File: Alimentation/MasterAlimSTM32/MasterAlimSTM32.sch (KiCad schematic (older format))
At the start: 74 parts, among them J1 Ext-Con, J10 Interf-Reg1, J11 AU Logic, J12 Interf-Reg2, J13 Interf-Reg3, J14 Interf-Reg4, J2 5V, J3 Bat. IN, J4 SWD, J5 Direct Out, J6 Reg 1, J7 Reg 2, J8 Reg 3, J9 Reg 4, SW1 SW_SPDT, U1 PTN78060W_EUW-7, U2 STM32F405RGTx, U3 ACS712xLCTR-20A, Y1 16Mhz

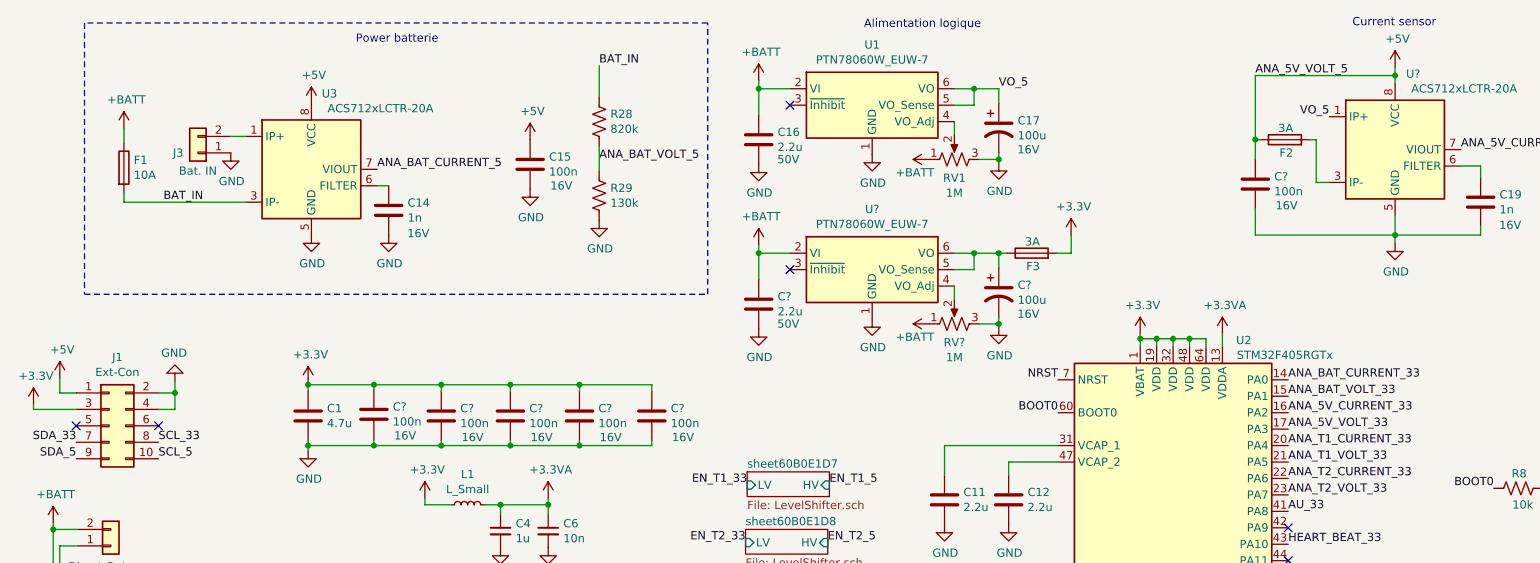
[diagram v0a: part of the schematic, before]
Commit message: Module alim ISO, clean master alim
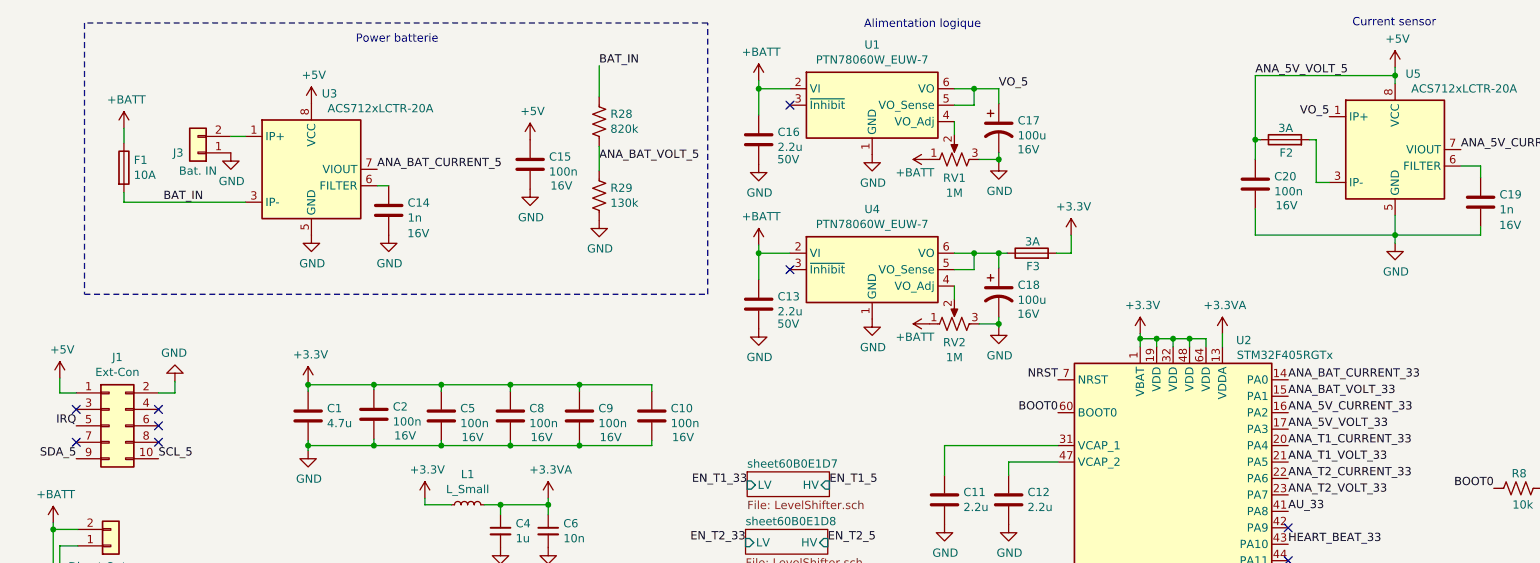
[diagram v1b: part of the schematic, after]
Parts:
- C14: LCSC C163169 -> (none)
- U1: footprint Module:Texas_EUW_R-PDSS-T7_THT -> ARIG:Texas_EUW_R-PDSS-T7_THT
- U4: renamed from U?; footprint Module:Texas_EUW_R-PDSS-T7_THT -> ARIG:Texas_EUW_R-PDSS-T7_THT
- gave numbers to parts that had none: 10
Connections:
- net +3V3: no longer J1.3 (Pin_3)
- net GND: no longer J1.4 (Pin_4)
- net SCL_33: no longer J1.8 (Pin_8)
- net SDA_33: no longer J1.7 (Pin_7)
- net IRQ: now reaches J1.5 (Pin_5)
- no-connect marks 32 -> 35
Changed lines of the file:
@@
 F 3 "~" H 2740 1700 50  0001 C CNN
 F 4 "16V" H 2920 1560 50  0000 C CNN "Tension"
-F 5 "C163169" H 2740 1700 50  0001 C CNN "LCSC"
-F 6 "C163169" H 2740 1700 50  0001 C CNN "LCSC Part"
+F 5 "C163169" H 2740 1700 50  0001 C CNN "LCSC Part"
 	1    2740 1700
 	1    0    0    -1
@@
 	1    0    0    -1
 $EndComp
-NoConn ~ 840  3010
 $Comp
 L MCU_ST_STM32F4:STM32F405RGTx U2
@@
 F 0 "U1" H 5680 1427 50  0000 C CNN
 F 1 "PTN78060W_EUW-7" H 5680 1336 50  0000 C CNN
-F 2 "Module:Texas_EUW_R-PDSS-T7_THT" H 5580 660 50  0001 C CNN
+F 2 "ARIG:Texas_EUW_R-PDSS-T7_THT" H 5580 660 50  0001 C CNN
 F 3 "https://www.ti.com/lit/ds/symlink/ptn78060w.pdf" H 5655 1110 50  0001 C CNN
 F 4 "" H 5680 1060 50  0001 C CNN "LCSC Bom"
@@
 Wire Wire Line
 	9500 4690 9580 4690
-Text Label 1340 3110 0    50   ~ 0
-SCL_33
-Text Label 840  3110 2    50   ~ 0
-SDA_33
-$Comp
-L power:+3.3V #PWR0148
-U 1 1 609CF06D
-P 580 2880
-F 0 "#PWR0148" H 580 2730 50  0001 C CNN
-F 1 "+3.3V" H 595 3053 50  0000 C CNN
-F 2 "" H 580 2880 50  0001 C CNN
-F 3 "" H 580 2880 50  0001 C CNN
-	1    580  2880
-	1    0    0    -1
-$EndComp
-Wire Wire Line
-	580  2880 580  2910
-Wire Wire Line
-	580  2910 840  2910
-Wire Wire Line
-	1440 2810 1440 2910
-Wire Wire Line
-	1440 2910 1340 2910
-Connection ~ 1440 2810
 $Comp
 L Device:R_US R4
@@
 	6510 3230 6510 3310
 $Comp
-L Device:C C?
+L Device:C C20
 U 1 1 5FC94B59
 P 8010 1540
-F 0 "C?" H 7895 1494 50  0000 R CNN
+F 0 "C20" H 7895 1494 50  0000 R CNN
 F 1 "100n" H 7895 1585 50  0000 R CNN
 F 2 "Capacitor_SMD:C_0603_1608Metric_Pad1.08x0.95mm_HandSolder" H 8048 1390 50  0001 C CNN
@@
 $EndComp
 $Comp
-L Device:C C?
+L Device:C C2
 U 1 1 5FC9E5DA
 P 2650 2940
-F 0 "C?" H 2535 2894 50  0000 R CNN
+F 0 "C2" H 2535 2894 50  0000 R CNN
 F 1 "100n" H 2535 2985 50  0000 R CNN
 F 2 "Capacitor_SMD:C_0603_1608Metric_Pad1.08x0.95mm_HandSolder" H 2688 2790 50  0001 C CNN
@@
 $EndComp
 $Comp
-L Device:C C?
+L Device:C C5
 U 1 1 5FC9F7C9
 P 3060 2950
-F 0 "C?" H 2945 2904 50  0000 R CNN
+F 0 "C5" H 2945 2904 50  0000 R CNN
 F 1 "100n" H 2945 2995 50  0000 R CNN
 F 2 "Capacitor_SMD:C_0603_1608Metric_Pad1.08x0.95mm_HandSolder" H 3098 2800 50  0001 C CNN
@@
 $EndComp
 $Comp
-L Device:C C?
+L Device:C C8
 U 1 1 5FCA0138
 P 3480 2950
-F 0 "C?" H 3365 2904 50  0000 R CNN
+F 0 "C8" H 3365 2904 50  0000 R CNN
 F 1 "100n" H 3365 2995 50  0000 R CNN
 F 2 "Capacitor_SMD:C_0603_1608Metric_Pad1.08x0.95mm_HandSolder" H 3518 2800 50  0001 C CNN
@@
 $EndComp
 $Comp
-L Device:C C?
+L Device:C C9
 U 1 1 5FCA09DF
 P 3900 2950
-F 0 "C?" H 3785 2904 50  0000 R CNN
+F 0 "C9" H 3785 2904 50  0000 R CNN
 F 1 "100n" H 3785 2995 50  0000 R CNN
 F 2 "Capacitor_SMD:C_0603_1608Metric_Pad1.08x0.95mm_HandSolder" H 3938 2800 50  0001 C CNN
@@
 $EndComp
 $Comp
-L Device:C C?
+L Device:C C10
 U 1 1 5FCA121E
 P 4340 2950
-F 0 "C?" H 4225 2904 50  0000 R CNN
+F 0 "C10" H 4225 2904 50  0000 R CNN
 F 1 "100n" H 4225 2995 50  0000 R CNN
 F 2 "Capacitor_SMD:C_0603_1608Metric_Pad1.08x0.95mm_HandSolder" H 4378 2800 50  0001 C CNN
@@
 $EndComp
 $Comp
-L Sensor_Current:ACS712xLCTR-20A U?
+L Sensor_Current:ACS712xLCTR-20A U5
 U 1 1 5FCD64E0
 P 8860 1330
-F 0 "U?" H 8970 1790 50  0000 C CNN
+F 0 "U5" H 8970 1790 50  0000 C CNN
 F 1 "ACS712xLCTR-20A" H 9280 1700 50  0000 C CNN
 F 2 "Package_SO:SOIC-8_3.9x4.9mm_P1.27mm" H 8960 980 50  0001 L CIN
@@
 $EndComp
 $Comp
-L ARIG:PTN78060W_EUW-7 U?
+L ARIG:PTN78060W_EUW-7 U4
 U 1 1 5FCDEF3A
 P 5680 2060
-F 0 "U?" H 5680 2427 50  0000 C CNN
+F 0 "U4" H 5680 2427 50  0000 C CNN
 F 1 "PTN78060W_EUW-7" H 5680 2336 50  0000 C CNN
-F 2 "Module:Texas_EUW_R-PDSS-T7_THT" H 5580 1660 50  0001 C CNN
+F 2 "ARIG:Texas_EUW_R-PDSS-T7_THT" H 5580 1660 50  0001 C CNN
 F 3 "https://www.ti.com/lit/ds/symlink/ptn78060w.pdf" H 5655 2110 50  0001 C CNN
 F 4 "" H 5680 2060 50  0001 C CNN "LCSC Bom"
@@
 $EndComp
 $Comp
-L Device:C C?
+L Device:C C13
 U 1 1 5FCE4144
 P 4990 2270
-F 0 "C?" H 5105 2316 50  0000 L CNN
+F 0 "C13" H 5105 2316 50  0000 L CNN
 F 1 "2.2u" H 5105 2225 50  0000 L CNN
 F 2 "Capacitor_SMD:C_1206_3216Metric_Pad1.33x1.80mm_HandSolder" H 5028 2120 50  0001 C CNN
@@
 $EndComp
 $Comp
-L Device:R_POT_US RV?
+L Device:R_POT_US RV2
 U 1 1 5FCE7969
 P 6180 2390
-F 0 "RV?" V 6067 2390 50  0000 C CNN
+F 0 "RV2" V 6067 2390 50  0000 C CNN
 F 1 "1M" V 5976 2390 50  0000 C CNN
 F 2 "Potentiometer_THT:Potentiometer_Bourns_3266Y_Vertical" H 6180 2390 50  0001 C CNN
@@
 $EndComp
 $Comp
-L Device:CP1 C?
+L Device:CP1 C18
 U 1 1 5FCED70C
 P 6450 2200
-F 0 "C?" H 6565 2246 50  0000 L CNN
+F 0 "C18" H 6565 2246 50  0000 L CNN
 F 1 "100u" H 6565 2155 50  0000 L CNN
 F 2 "Capacitor_SMD:CP_Elec_6.3x5.4" H 6450 2200 50  0001 C CNN
@@
 	1    0    0    -1
 $EndComp
+Text Label 840  3010 2    50   ~ 0
+IRQ
+NoConn ~ 840  2910
+NoConn ~ 1340 2910
+NoConn ~ 840  3110
+NoConn ~ 1340 3110
 $EndSCHEMATC
